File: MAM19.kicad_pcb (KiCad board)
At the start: 2 copper layers, 94 parts, among them J1001 PWM IR2127, J1002 PWM IR2127, J401 USART, J601 RJ45, J602 RJ45, Q901 IXFN420N10T, U201 MCP2551-I/SN, U202 MCP2515-xSO, U401 ATMEGA328P-PU, U501 LM7805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

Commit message: Componentes TUDO
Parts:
- removed J+18Controle1, JGND1-1: Controle, Connector_PinHeader_2.54mm:PinHeader_2x02_P2.54mm_Vertical
- removed J+18Driver1, JGND1-2: Driver, Connector_PinHeader_2.54mm:PinHeader_2x02_P2.54mm_Vertical
- removed J1001, J1002: PWM IR2127, Connector_PinHeader_2.54mm:PinHeader_1x02_P2.54mm_Vertical
- added J06: PWM/IR C, Connector_PinHeader_2.54mm:PinHeader_1x04_P2.54mm_Vertical, F.Cu at (44.5, 123.0)
- added J101: GNDC1, Connector_PinHeader_2.54mm:PinHeader_2x02_P2.54mm_Vertical, F.Cu at (24.0, 73.0)
- added J102: GNDC2, Connector_PinHeader_2.54mm:PinHeader_2x02_P2.54mm_Vertical, F.Cu at (60.0, 65.0)
- added J103: GNDD1, Connector_PinHeader_2.54mm:PinHeader_2x02_P2.54mm_Vertical, B.Cu at (74.6, 49.9)
- added J104: GNDD2, Connector_PinHeader_2.54mm:PinHeader_2x02_P2.54mm_Vertical, B.Cu at (110.7, 41.9)
- added J105: PWM/IR D, Connector_PinHeader_2.54mm:PinHeader_1x04_P2.54mm_Vertical, B.Cu at (95.1, 99.8)
- added J107: HOLD1, Connector_PinHeader_2.54mm:PinHeader_2x02_P2.54mm_Vertical, F.Cu at (121.1, 25.4)
- added J108: HOLD2, Connector_PinHeader_2.54mm:PinHeader_2x02_P2.54mm_Vertical, F.Cu at (110.7, 25.3)
- added J181: +18C, Connector_PinHeader_2.54mm:PinHeader_2x02_P2.54mm_Vertical, F.Cu at (24.0, 65.0)
- added J182: +18D, Connector_PinHeader_2.54mm:PinHeader_2x02_P2.54mm_Vertical, B.Cu at (74.6, 41.9)
- added J701: DRAIND, Connector_PinHeader_2.54mm:PinHeader_2x02_P2.54mm_Vertical, F.Cu at (161.8, 25.4)
- added J702: GATED, Connector_PinHeader_2.54mm:PinHeader_2x02_P2.54mm_Vertical, F.Cu at (161.8, 101.6)
- added J703: SOURCED, Connector_PinHeader_2.54mm:PinHeader_2x02_P2.54mm_Vertical, F.Cu at (121.1, 101.6)
- added J704: DRAINCH, Connector_PinHeader_2.54mm:PinHeader_2x02_P2.54mm_Vertical, F.Cu at (70.0, 25.3)
- added J705: GATECH, Connector_PinHeader_2.54mm:PinHeader_2x02_P2.54mm_Vertical, F.Cu at (70.0, 101.5)
- added J706: SOURCECH, Connector_PinHeader_2.54mm:PinHeader_2x02_P2.54mm_Vertical, F.Cu at (110.7, 101.5)
- C901: moved to F.Cu
- moved C801 236.8 mm to (38.1, 147.7)
- moved C802 236.8 mm to (112.0, 147.7)
- moved C803 236.8 mm to (149.0, 147.7)
- moved C805 236.8 mm to (75.1, 147.7)
- moved C806 236.8 mm to (222.9, 147.7)
- moved C804 236.8 mm to (186.0, 147.7)
- moved DZ701 168.6 mm to (80.2, 95.5), turned to 90 degrees
- moved J601 168.3 mm to (33.3, 33.5), turned to 180 degrees
- moved U701 168.2 mm to (86.5, 75.8), turned to 180 degrees
- moved C701 159.2 mm to (92.5, 73.0)
- moved R707 157.2 mm to (83.3, 98.4), turned to 180 degrees
- moved J602 155.2 mm to (54.2, 33.5), turned to 180 degrees
- moved C703 154.4 mm to (87.6, 80.5), turned to 90 degrees
- moved F501 153.9 mm to (29.5, 48.2), turned to 90 degrees
- moved D201 153.4 mm to (35.8, 44.2), turned to 90 degrees
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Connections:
- D601 pad 2: Net-(D601-Pad2) -> /POWER SUPPLY +15V/+18V_IN
- U702 pad 9: (no net) -> GND
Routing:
- net +15V: track 9.39 -> 51.5 mm, vias 0 -> 5
- net Net-(C501-Pad1): track 14.7 -> 43.3 mm
- net GND: track 324.2 -> 304.0 mm
- net Net-(C703-Pad2): track 0.00 -> 17.7 mm, vias 0 -> 2
- net /POWER SUPPLY +15V/+18V_IN: track 60.6 -> 49.1 mm
- net Net-(R705-Pad2): track 0.00 -> 11.0 mm
- net Net-(R701-Pad2): track 0.00 -> 10.4 mm
- net +5V: track 158.6 -> 150.7 mm, vias 6 -> 4
- net Net-(C601-Pad1): track 4.32 -> 11.5 mm
- net Net-(C702-Pad2): track 0.00 -> 6.25 mm
- net Net-(R704-Pad1): track 0.00 -> 4.21 mm
- net /driver/IR2127_FAULT: track 0.00 -> 3.41 mm, vias 0 -> 1
- net /driver/PWM: track 0.00 -> 3.40 mm, vias 0 -> 1
- net Net-(R406-Pad1): track 3.27 -> 0.00 mm
- net Net-(D702-Pad2): track 0.00 -> 2.00 mm
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- added copper zone on B.Cu, net +15V
- added copper zone on F.Cu, net +15V
- added copper zone on F.Cu, net GND
- added copper zone on B.Cu, net Net-(D702-Pad2)
- added copper zone on B.Cu, net Net-(D703-Pad1)

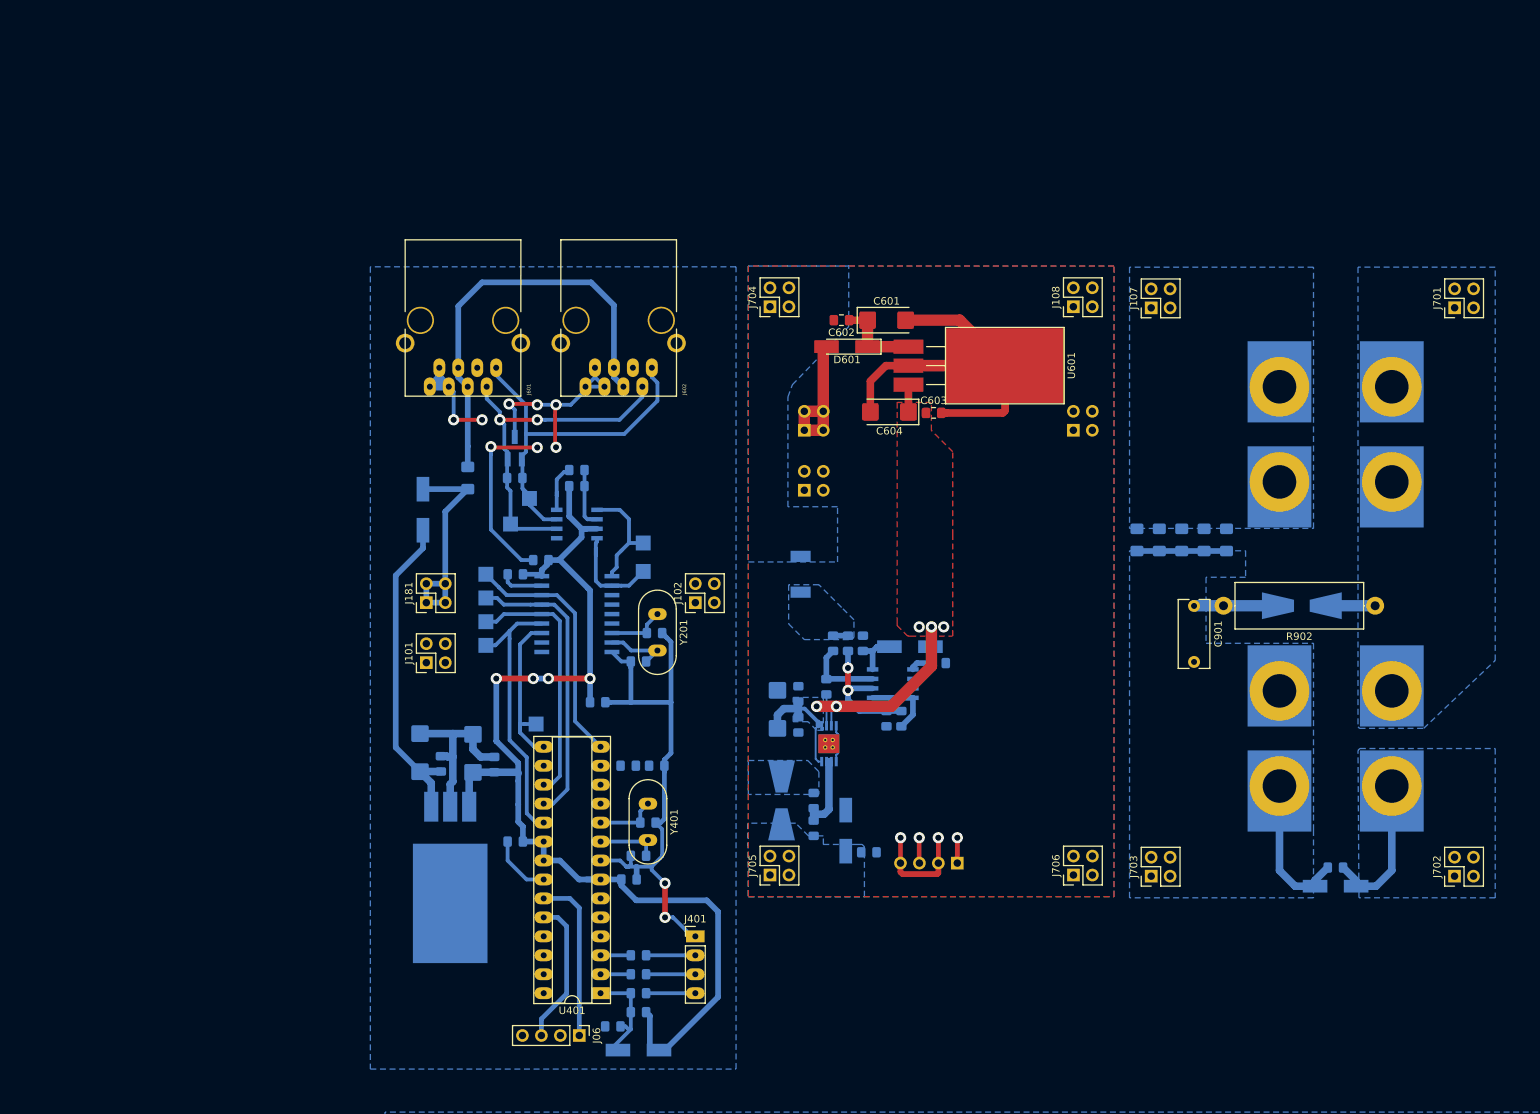
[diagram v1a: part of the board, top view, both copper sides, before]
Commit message: Mosfet driver PCB
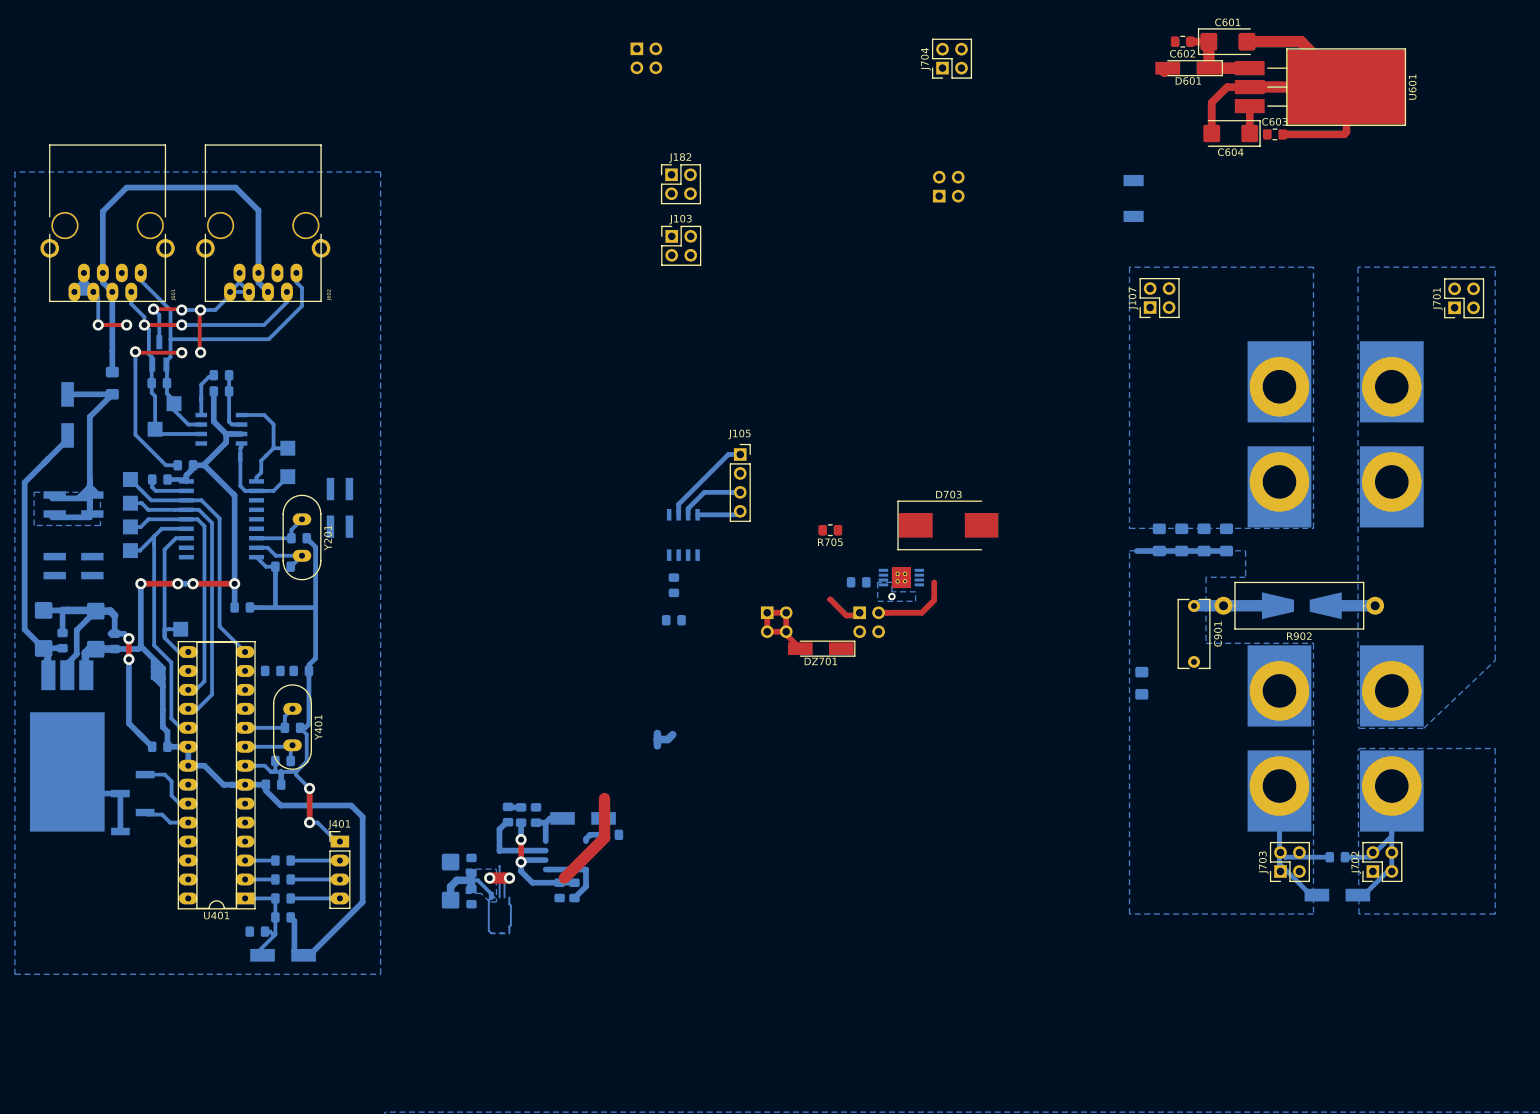
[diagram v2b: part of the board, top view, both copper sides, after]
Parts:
- D703: footprint Diode_SMD:D_SMB-SMC_Universal_Handsoldering -> Diode_SMD:D_SMC_Handsoldering; moved to F.Cu
- DZ701, J103, J182, R705: moved to F.Cu
- J06: footprint Connector_PinHeader_2.54mm:PinHeader_1x04_P2.54mm_Vertical -> Connector_PinHeader_2.54mm:PinHeader_1x04_P2.54mm_Vertical_SMD_Pin1Left; moved to B.Cu
- J101, J102, J181: footprint Connector_PinHeader_2.54mm:PinHeader_2x02_P2.54mm_Vertical -> Connector_PinSocket_2.54mm:PinSocket_2x02_P2.54mm_Vertical_SMD; moved to B.Cu
- J105: footprint Connector_PinHeader_2.54mm:PinHeader_1x04_P2.54mm_Vertical -> Connector_PinSocket_2.54mm:PinSocket_1x04_P2.54mm_Vertical; moved to F.Cu
- J108, J705, J706: moved to B.Cu
- moved J108 67.9 mm to (52.2, -9.26), turned to 270 degrees
- moved J06 67.5 mm to (-15.4, 91.8), turned to 180 degrees
- moved D702 67.3 mm to (118.7, 10.8)
- moved J105 62.0 mm to (66.0, 45.1), turned to 0 degrees
- moved U601 59.0 mm to (135.6, -6.67)
- moved C602 59.0 mm to (125.3, -10.2)
- moved C603 59.0 mm to (137.7, 2.21)
- moved D601 59.0 mm to (126.1, -6.67)
- moved C601 59.0 mm to (131.4, -10.2)
- moved C604 59.0 mm to (131.8, 2.08)
- moved U501 54.2 mm to (-26.7, 75.9)
- moved J706 54.0 mm to (69.7, 66.3), turned to 270 degrees
- moved C503 53.5 mm to (-17.8, 70.1)
- moved C502 53.3 mm to (-24.8, 70.0)
- moved C504 53.2 mm to (-20.3, 68.6)
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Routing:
- net GND: track 304.0 -> 349.8 mm, vias 12 -> 13
- net /chopper/GATE: track 20.2 -> 46.6 mm
- net /MCU/PWM: track 22.4 -> 8.78 mm
- net /MCU/IR_2127_FAULT: track 20.2 -> 6.97 mm
- net +5V: track 150.7 -> 160.6 mm
- net /driver/PWM: track 3.40 -> 12.4 mm, vias 1 -> 0
- net +15V: track 51.5 -> 44.1 mm, vias 5 -> 2
- net /POWER SUPPLY +15V/+18V_IN: track 49.1 -> 42.3 mm
- net Net-(R705-Pad2): track 11.0 -> 4.62 mm
- net /driver/IR2127_FAULT: track 3.41 -> 8.72 mm, vias 1 -> 0
- added copper zone on B.Cu, net /POWER SUPPLY +15V/+18V_IN
- removed copper zone on F.Cu, net +15V
- removed copper zone on F.Cu, net GND
- removed copper zone on B.Cu, net Net-(D702-Pad2)
- removed copper zone on B.Cu, net Net-(D703-Pad1)

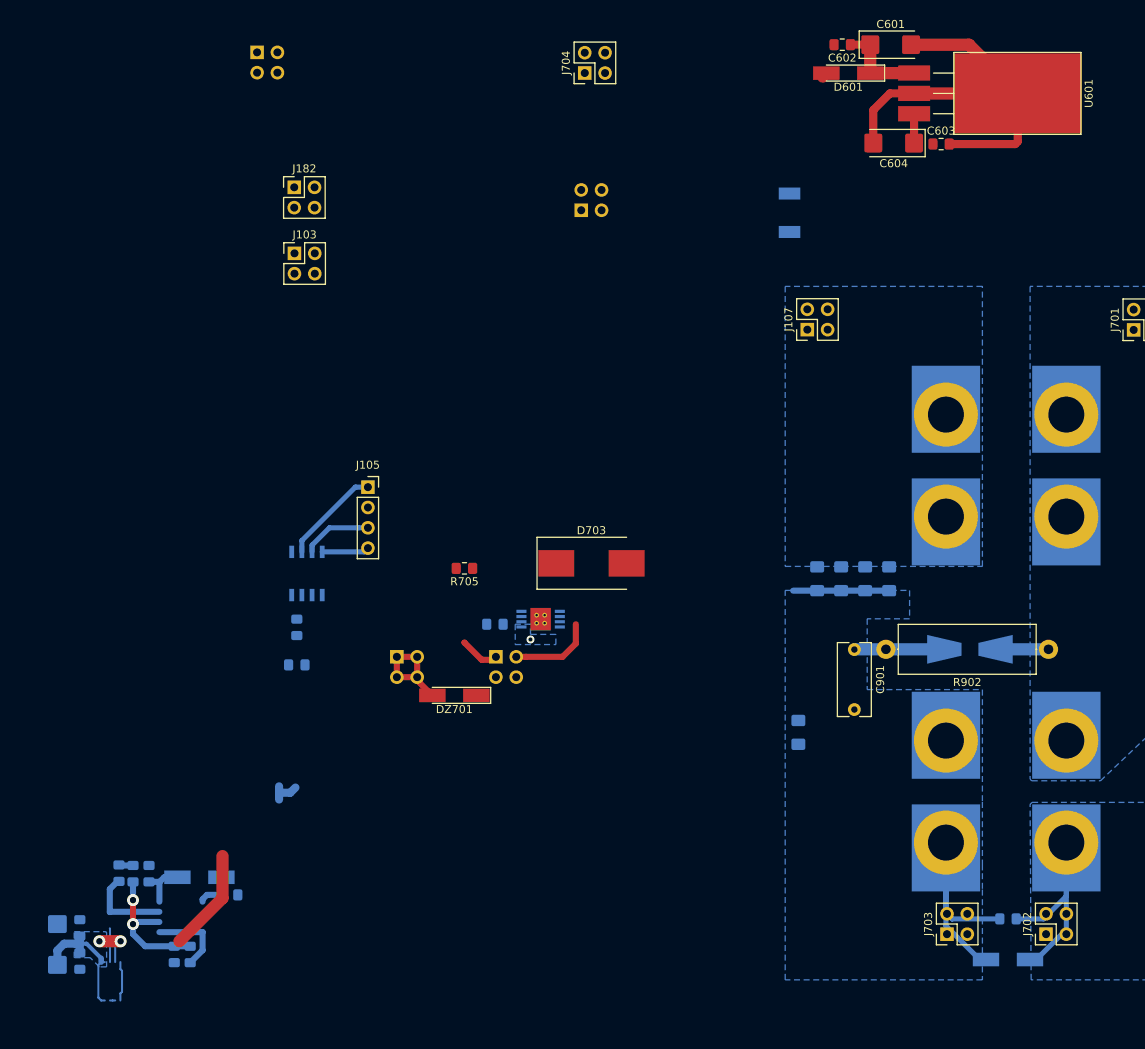
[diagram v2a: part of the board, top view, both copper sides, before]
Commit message: small updates driver Mosfet
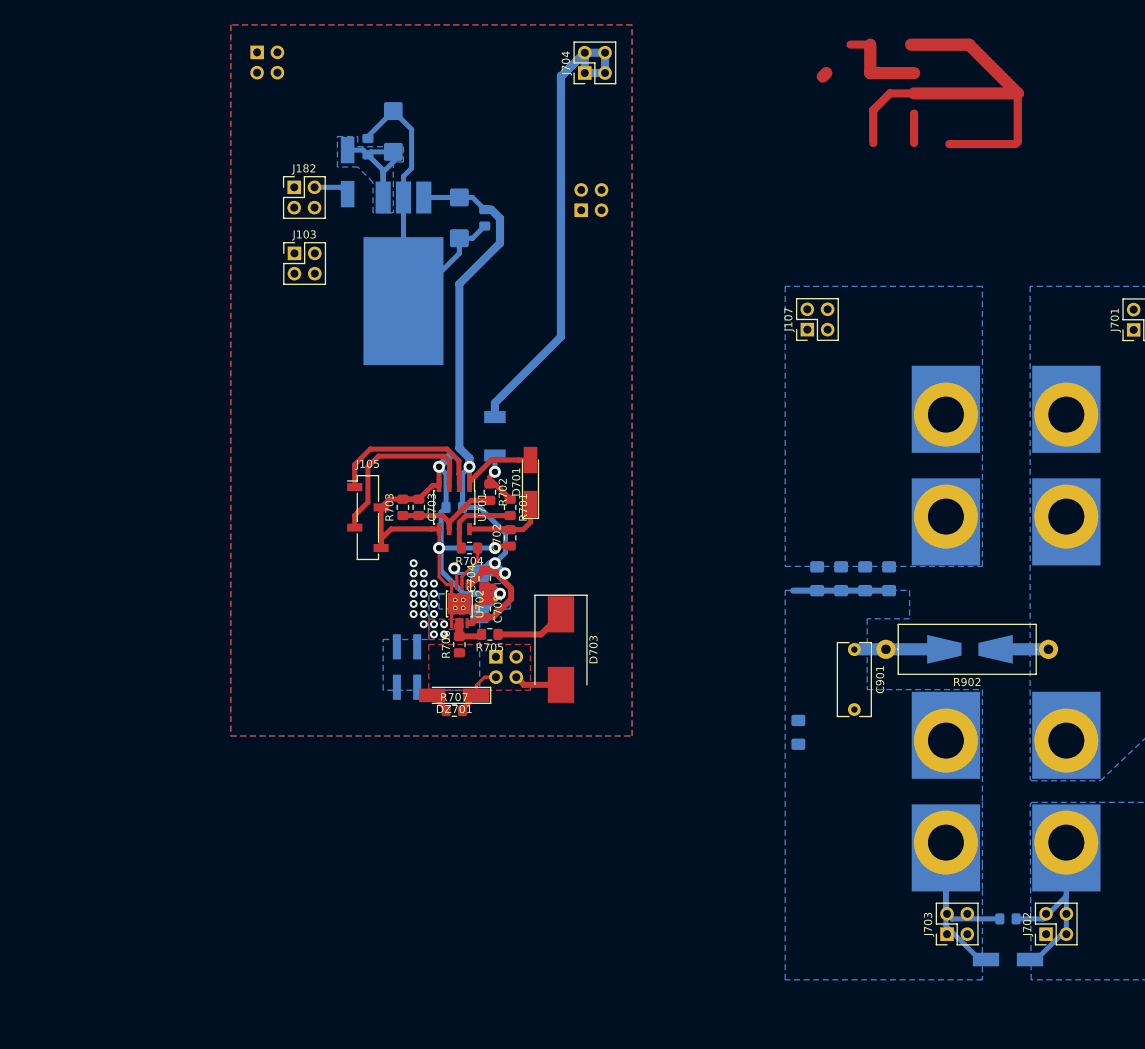
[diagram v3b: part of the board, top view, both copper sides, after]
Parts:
- C601, C602, C603, C604, D601, U601: moved to B.Cu
- C702, C703, C704, C705, D701, R701, R702, R703, R704, R706, R707, U701, U702: moved to F.Cu
- J105: footprint Connector_PinSocket_2.54mm:PinSocket_1x04_P2.54mm_Vertical -> Connector_PinSocket_2.54mm:PinSocket_1x04_P2.54mm_Vertical_SMD_Pin1Left
- J706: footprint Connector_PinHeader_2.54mm:PinHeader_2x02_P2.54mm_Vertical -> Connector_PinHeader_2.54mm:PinHeader_2x02_P2.54mm_Vertical_SMD
- moved U601 69.7 mm to (67.9, 10.2), turned to 0 degrees
- moved C706 68.6 mm to (80.0, 58.4), turned to 90 degrees
- moved C705 67.1 mm to (80.6, 60.3), turned to 270 degrees
- moved R701 66.9 mm to (83.8, 47.6)
- moved C704 66.9 mm to (80.6, 56.5), turned to 90 degrees
- moved R702 65.3 mm to (81.3, 45.7)
- moved D701 64.5 mm to (86.4, 44.5), turned to 90 degrees
- moved D601 63.8 mm to (63.5, 5.71), turned to 270 degrees
- moved C601 63.1 mm to (69.2, 0.64), turned to 90 degrees
- moved C703 62.8 mm to (72.4, 47.6), turned to 270 degrees
- moved R703 62.8 mm to (70.4, 47.6), turned to 90 degrees
- moved C702 61.6 mm to (83.8, 51.4), turned to 90 degrees
- moved C602 60.7 mm to (66.0, 2.54), turned to 90 degrees
- moved C603 57.8 mm to (80.6, 11.4), turned to 270 degrees
- moved C701 56.0 mm to (76.8, 47.6), turned to 180 degrees
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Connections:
- U702 pad 9: GND -> (no net)
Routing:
- net GND: track 349.8 -> 458.3 mm, vias 13 -> 36
- net /chopper/-MOTOR: track 7.78 -> 72.8 mm
- net +15V: track 44.1 -> 106.6 mm, vias 2 -> 4
- net Net-(C601-Pad1): track 11.5 -> 30.5 mm
- net /driver/IR2127_FAULT: track 8.72 -> 22.4 mm
- net Net-(D703-Pad1): track 0.00 -> 8.90 mm
- net /driver/PWM: track 12.4 -> 20.4 mm
- net Net-(D702-Pad2): track 2.00 -> 7.15 mm, vias 0 -> 1
- net /POWER SUPPLY +15V/+18V_IN: track 42.3 -> 46.8 mm
- net Net-(R705-Pad2): track 4.62 -> 8.62 mm
- net Net-(C702-Pad2): track 6.25 -> 9.69 mm
- net Net-(C703-Pad2): track 17.7 -> 15.1 mm, vias 2 -> 0
- net /chopper/GATE: track 46.6 -> 44.4 mm
- net Net-(R701-Pad2): track 10.4 -> 12.6 mm
- net Net-(R704-Pad1): track 4.21 -> 5.40 mm
- added copper zone on F.Cu, net /chopper/GATE
- added copper zone on F.Cu, net GND
- added copper zone on B.Cu, net Net-(C601-Pad1)
- removed copper zone on B.Cu, net +15V

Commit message: update
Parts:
- J704: moved to B.Cu
- moved J706 23.4 mm to (57.8, 87.0)
- moved J705 22.8 mm to (93.5, 86.0)
- moved C703 19.7 mm to (73.0, 67.3)
- moved C602 19.7 mm to (66.7, 22.2)
- moved C702 19.7 mm to (84.5, 71.1)
- moved C704 19.7 mm to (81.3, 76.2)
- moved C705 19.7 mm to (81.3, 80.0)
- moved C706 19.7 mm to (80.6, 78.1)
- moved D701 19.7 mm to (87.0, 64.1)
- moved D702 19.7 mm to (82.5, 58.4)
- moved J103 19.7 mm to (57.5, 35.6)
- moved J104 19.7 mm to (93.3, 30.2)
- moved J182 19.7 mm to (57.5, 27.3)
- moved R701 19.7 mm to (84.5, 67.3)
- moved R702 19.7 mm to (81.9, 65.4)
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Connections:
- U702 pad 9: (no net) -> GND
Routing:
- net GND: track 458.3 -> 415.7 mm, vias 36 -> 58
- net +15V: track 106.6 -> 82.2 mm
- net /chopper/-MOTOR: track 72.8 -> 61.1 mm
- net Net-(C601-Pad1): track 30.5 -> 19.0 mm
- net Net-(D703-Pad1): track 8.90 -> 0.00 mm
- net /chopper/GATE: track 44.4 -> 36.1 mm
- net /POWER SUPPLY +15V/+18V_IN: track 46.8 -> 46.2 mm
- net (no net): vias 0 -> 52

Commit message: Driver layout and snubber
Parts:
- removed C901: C_Small, Capacitor_THT:C_Rect_L9.0mm_W4.0mm_P7.50mm_MKT
- removed D901: ES3B, Diode_SMD:D_SMB-SMC_Universal_Handsoldering
- removed R902: 4R7, Resistor_THT:R_Axial_DIN0617_L17.0mm_D6.0mm_P20.32mm_Horizontal
- moved C904 21.8 mm to (130.2, 56.5)
- moved R901 4.07 mm to (149.2, 101.6)
- moved DZ901 3.81 mm to (149.9, 104.1)
- moved C902 3.65 mm to (127.5, 56.5)
- moved C905 3.28 mm to (124.9, 56.5)
- moved D703 3.18 mm to (88.3, 83.2), turned to 270 degrees
- moved C903 2.91 mm to (122.3, 56.5)
- moved C906 2.54 mm to (119.7, 56.5)
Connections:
- U702 pad 9: GND -> (no net)
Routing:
- net GND: track 415.7 -> 450.9 mm, vias 58 -> 41
- net +15V: track 82.2 -> 103.0 mm
- net /chopper/GATE: track 36.1 -> 50.0 mm
- net Net-(C901-Pad1): track 11.3 -> 0.00 mm
- net +36V: track 0.00 -> 10.5 mm
- net Net-(D703-Pad1): track 0.00 -> 7.50 mm
- net /chopper/-MOTOR: track 61.1 -> 66.2 mm
- net Net-(R406-Pad1): track 0.00 -> 2.68 mm
- net Net-(D403-Pad2): track 0.00 -> 1.78 mm
- net (no net): vias 52 -> 0
